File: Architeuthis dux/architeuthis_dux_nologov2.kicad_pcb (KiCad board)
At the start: 2 copper layers, 129.9 x 95.6 mm, 19 parts

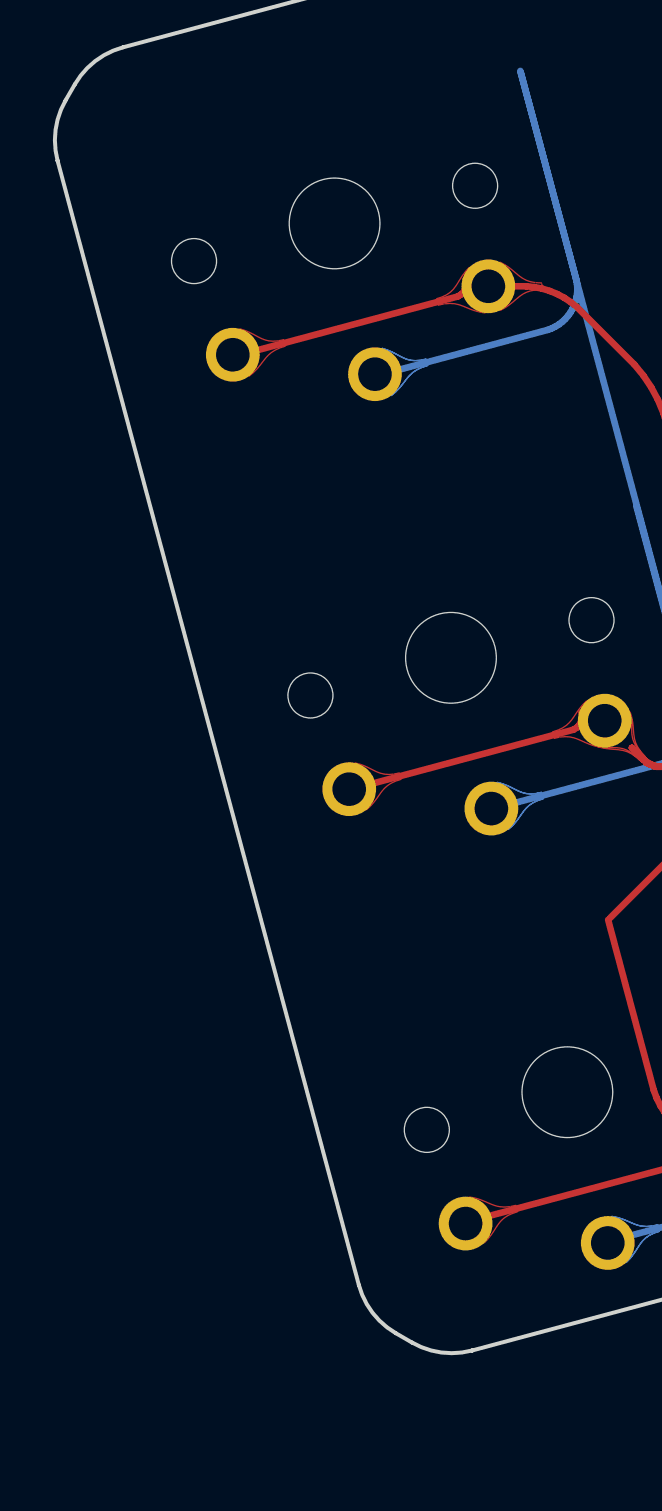
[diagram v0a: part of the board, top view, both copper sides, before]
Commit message: Remove phantom drill holes
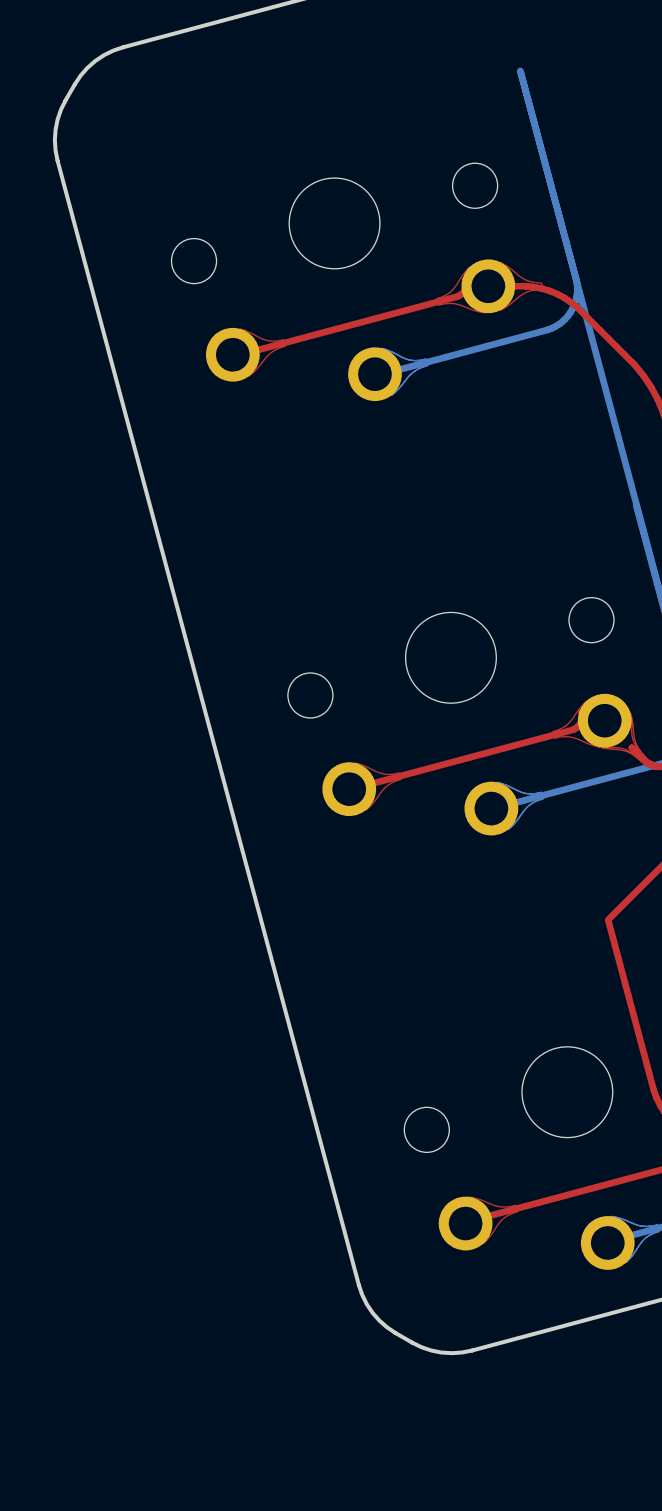
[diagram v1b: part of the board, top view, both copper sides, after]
